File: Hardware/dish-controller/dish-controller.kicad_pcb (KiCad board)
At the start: 4 copper layers, 165 x 70 mm, 54 parts, among them J1 12V-IN, J2 5V-IN, J3 Encoder_Conn, J4 Encoder_Conn, J5 AZ-OUT, J6 EL-OUT, Q5 BSS138, Q6 BSS138, Q7 BSS138, Q8 BSS138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

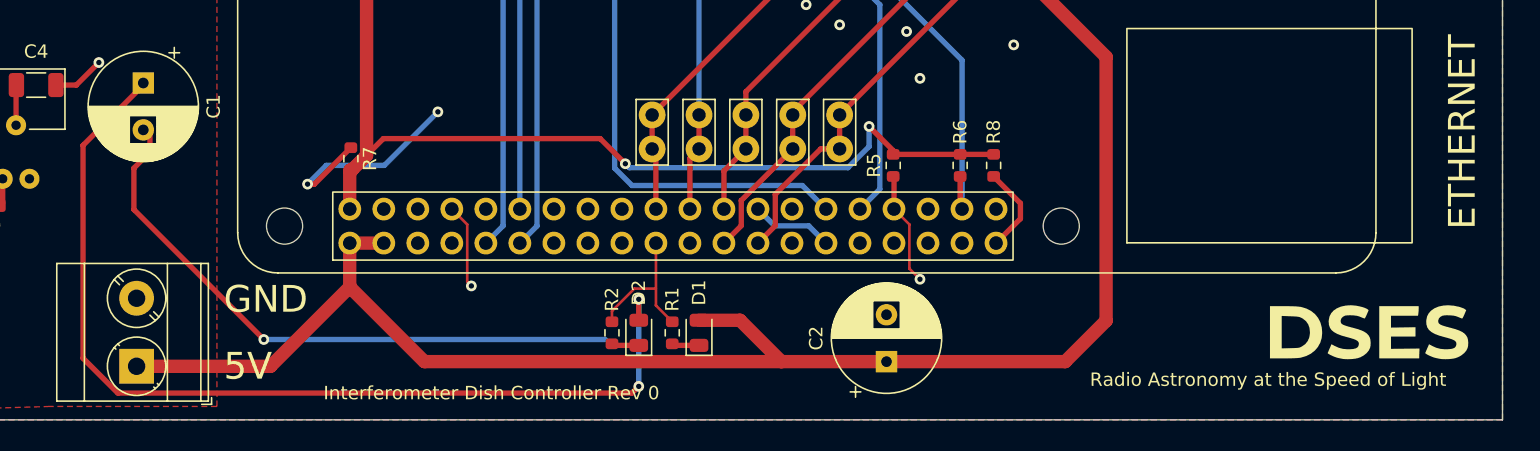
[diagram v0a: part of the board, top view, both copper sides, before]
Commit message: Dish Controller: Added I2C header
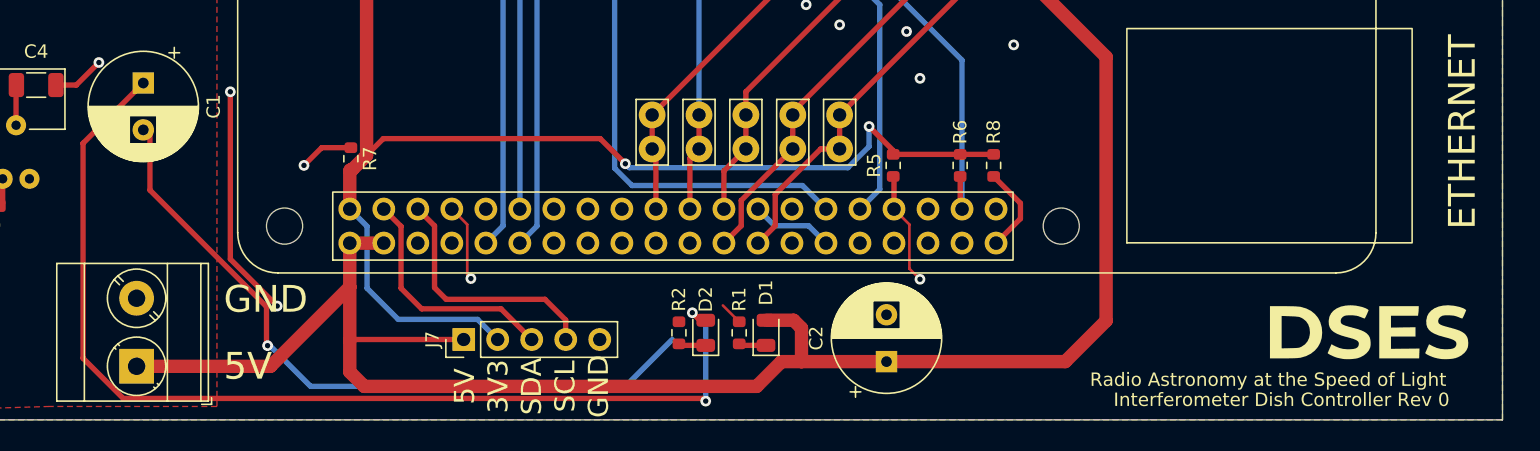
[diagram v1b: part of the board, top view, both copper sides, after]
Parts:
- added J7: Conn_01x05_Male, Connector_PinHeader_2.54mm:PinHeader_1x05_P2.54mm_Vertical, F.Cu at (105.4, 104.0)
- moved D1 5.00 mm to (128.0, 103.5)
- moved D2 5.00 mm to (123.5, 103.5)
- moved R1 5.00 mm to (126.0, 103.5)
- moved R2 5.00 mm to (121.5, 103.5)
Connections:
- U1 pad 3: /PWM1 -> /GPIO_2
- U1 pad 32: unconnected-(U1-Pad32) -> /PWM2
- U1 pad 36: unconnected-(U1-Pad36) -> /PWM1
- U1 pad 5: /PWM2 -> /GPIO_3
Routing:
- net /PWM1: track 34.1 -> 88.3 mm, vias 0 -> 2
- net /PWM2: track 76.3 -> 98.3 mm
- net /GPIO_3: track 0.00 -> 18.6 mm
- net +3V3: track 147.4 -> 165.2 mm
- net /GPIO_2: track 0.00 -> 17.8 mm
- net +5V: track 285.1 -> 296.9 mm
- net /A22: track 130.8 -> 120.2 mm
- net +12V: track 73.3 -> 78.5 mm
- net /A21: track 83.0 -> 80.3 mm, vias 2 -> 1
- net GND: track 114.6 -> 112.2 mm
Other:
- board text added: "3V3"
- board text added: "SCL"
- board text added: "SDA"

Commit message: Dish Controller: Plot
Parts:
- Q5, Q6, Q7, Q8: footprint Package_TO_SOT_SMD:SOT-23 -> Package_TO_SOT_SMD:SOT-323_SC-70
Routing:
- net GND: track 112.2 -> 110.4 mm
- net +12V: track 78.5 -> 79.1 mm
